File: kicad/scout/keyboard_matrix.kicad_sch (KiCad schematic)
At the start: 50 parts, among them SW1 SPST, SW10 SPST, SW11 SPST, SW12 SPST, SW13 SPST, SW14 SPST, SW15 SPST, SW16 SPST, SW17 SPST, SW18 SPST, SW19 SPST, SW2 SPST, SW20 SPST, SW21 SPST, SW22 SPST, SW23 SPST, SW24 SPST, SW25 SPST, SW3 SPST, SW4 SPST, SW5 SPST, SW6 SPST, SW7 SPST, SW8 SPST, SW9 SPST

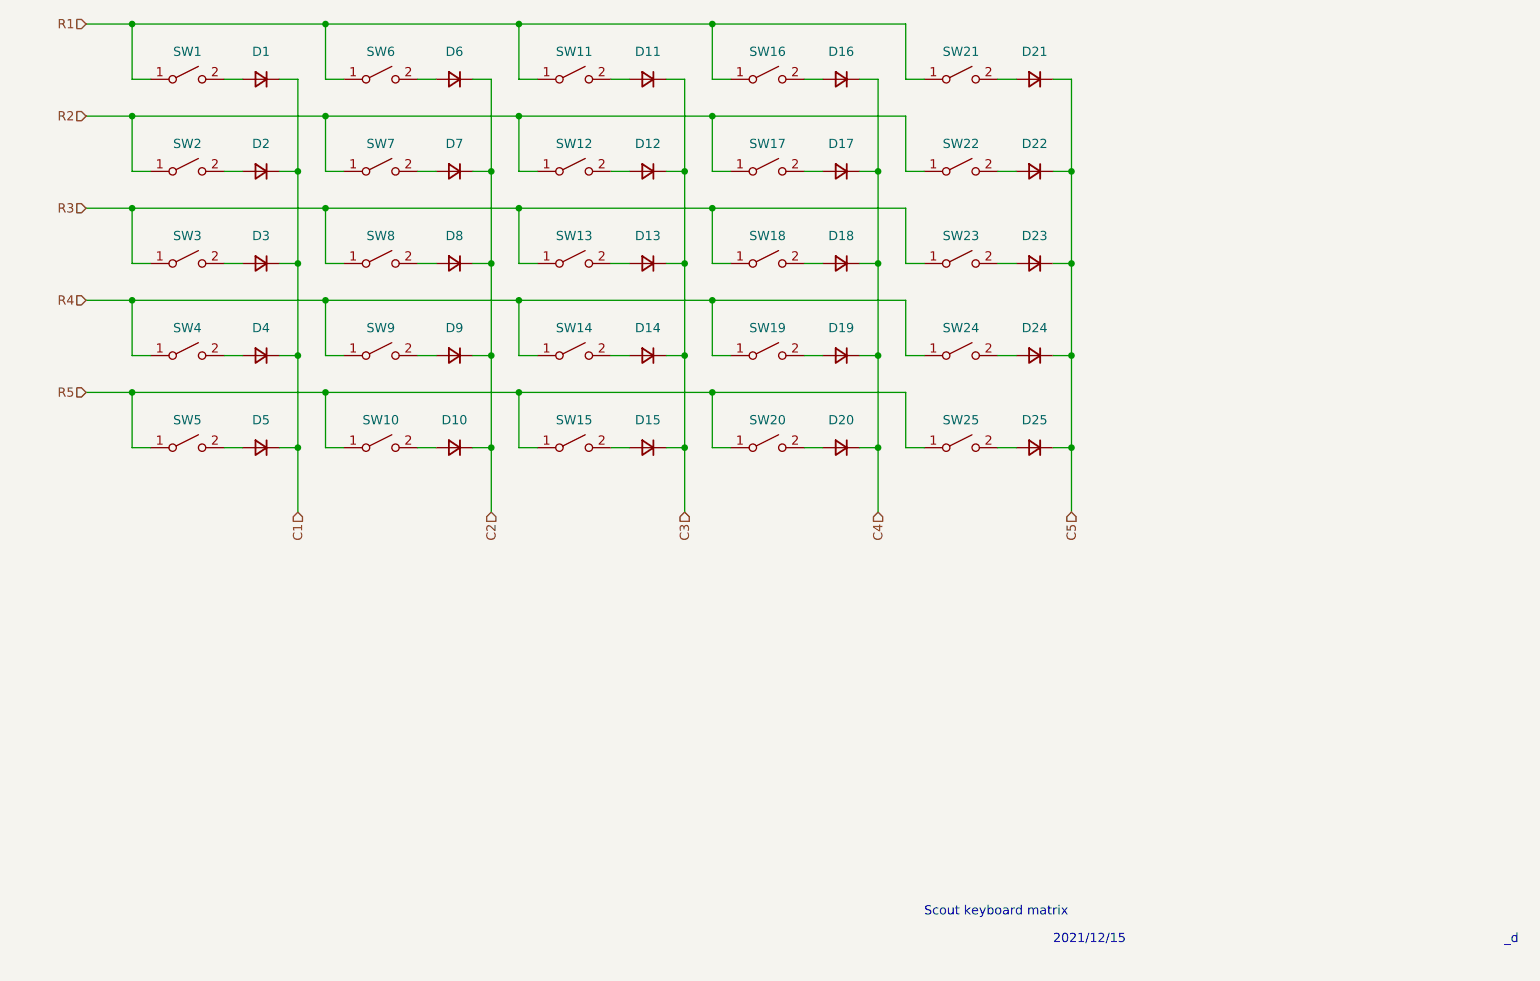
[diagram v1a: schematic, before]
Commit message: Update schematic
Should be no changes to function or PCB...

* Note pin assignments
* Tidy RV2 and RV3 voltage dividers
* Have MIDI read left to right
* Specify 1N4148 diodes

And add to readme
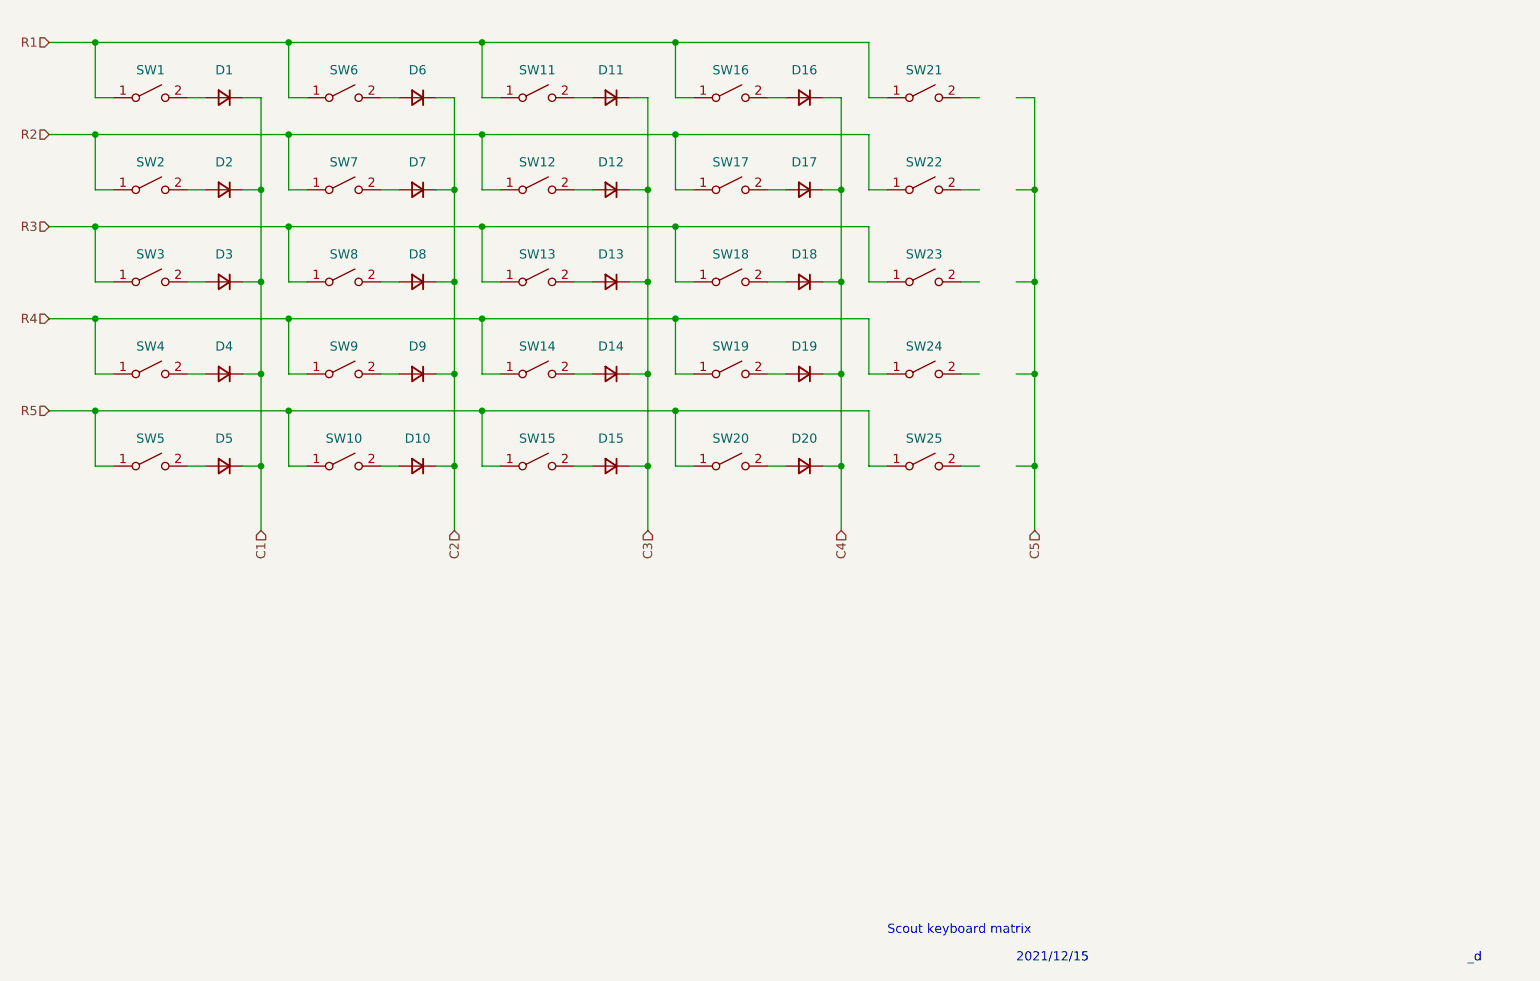
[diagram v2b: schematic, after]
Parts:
- removed D21, D22, D23, D24, D25: D, Diode_THT:D_DO-41_SOD81_P10.16mm_Horizontal, symbol Device:D_Small
- D1, D10, D11, D12, D13, D14, D15, D16, D17, D18, D19, D2, D20, D3, D4, D5, D6, D7, D8, D9: value D -> 1N4148
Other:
- moved on the sheet: D1, SW1, SW10, SW11, SW12, SW13, SW14, SW15, SW16, SW17, SW18, SW19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

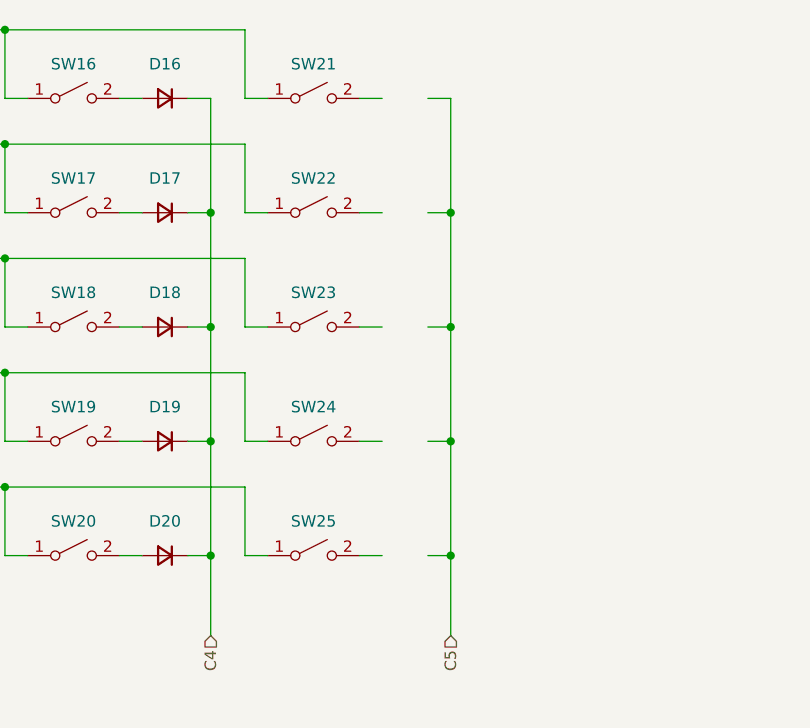
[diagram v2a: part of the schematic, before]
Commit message: Try to reduce noise and other refinements
* Add decoupling cap before amp
* Add snubber circuit after amp
* Consider bass boost for next rev
* Self-document pin connection assignments in schematic
* Move branding text beyond key area
* Reverse power switch direction
* Enlarge UART hookup labels
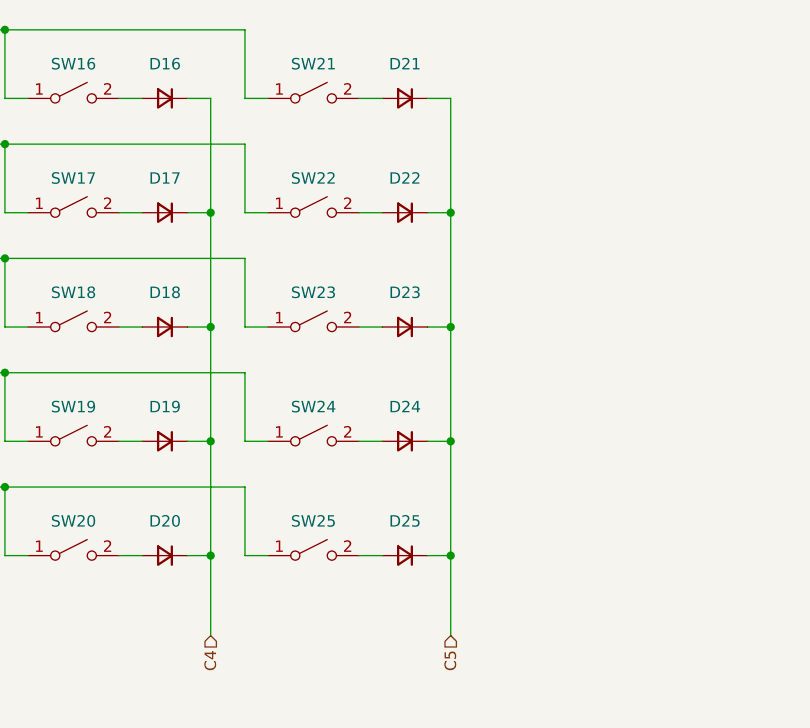
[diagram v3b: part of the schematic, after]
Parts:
- added D21, D22, D23, D24, D25: 1N4148, Diode_THT:D_DO-41_SOD81_P10.16mm_Horizontal, symbol Device:D_Small
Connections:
- net C5: now also D21.1 (K), D22.1 (K), D23.1 (K), D24.1 (K), D25.1 (K)
- net at SW21.2 (B): now also D21.2 (A)
- net at SW22.2 (B): now also D22.2 (A)
- net at SW23.2 (B): now also D23.2 (A)
- net at SW24.2 (B): now also D24.2 (A)
- net at SW25.2 (B): now also D25.2 (A)
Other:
- title: (none) -> SCOUT
